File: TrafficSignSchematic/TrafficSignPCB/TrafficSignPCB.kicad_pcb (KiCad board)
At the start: 2 copper layers, 106.7 x 90.4 mm, 33 parts, among them J1 IDC connector, J2 3.96mm pitch 4-pin polarized 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, J3 Power In, U1 ATmega328P-PU, U2 SIM800L, Y1 16MHz

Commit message: Forgot to save...
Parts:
- moved R5 10.4 mm to (95.2, 151.6), turned to 180 degrees
- moved R4 2.55 mm to (108.7, 138.9)
- moved R6 2.55 mm to (101.1, 142.7)
- moved R3 2.55 mm to (101.1, 135.4)
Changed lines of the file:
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@@
   )
   (module Resistor_THT:R_Axial_DIN0204_L3.6mm_D1.6mm_P7.62mm_Horizontal (layer F.Cu)
-    (at 98.552 135.636)
+    (at 101.092 135.382)
     (descr "Resistor, Axial_DIN0204 series, Axial, Horizontal, pin pitch=7.62mm, 0.167W, length*diameter=3.6*1.6mm^2, http://cdn-reichelt.de/documents/datenblatt/B400/1_4W%23YAG.pdf")
     (tags "Resistor Axial_DIN0204 series Axial Horizontal pin pitch 7.62mm 0.167W length 3.6mm diameter 1.6mm")
@@
   )
   (module Resistor_THT:R_Axial_DIN0204_L3.6mm_D1.6mm_P7.62mm_Horizontal (layer F.Cu)
-    (at 106.172 139.192 180)
+    (at 108.712 138.938 180)
     (descr "Resistor, Axial_DIN0204 series, Axial, Horizontal, pin pitch=7.62mm, 0.167W, length*diameter=3.6*1.6mm^2, http://cdn-reichelt.de/documents/datenblatt/B400/1_4W%23YAG.pdf")
     (tags "Resistor Axial_DIN0204 series Axial Horizontal pin pitch 7.62mm 0.167W length 3.6mm diameter 1.6mm")
@@
   )
   (module Resistor_THT:R_Axial_DIN0204_L3.6mm_D1.6mm_P7.62mm_Horizontal (layer F.Cu)
-    (at 88.138 144.018 270)
+    (at 95.25 151.638 180)
     (descr "Resistor, Axial_DIN0204 series, Axial, Horizontal, pin pitch=7.62mm, 0.167W, length*diameter=3.6*1.6mm^2, http://cdn-reichelt.de/documents/datenblatt/B400/1_4W%23YAG.pdf")
     (tags "Resistor Axial_DIN0204 series Axial Horizontal pin pitch 7.62mm 0.167W length 3.6mm diameter 1.6mm")
-    (fp_text reference R5 (at 3.81 -1.92 90) (layer F.SilkS)
+    (fp_text reference R5 (at 3.81 -1.92) (layer F.SilkS)
       (effects (font (size 1 1) (thickness 0.15)))
     )
-    (fp_text value 10k (at 3.81 1.92 90) (layer F.Fab)
+    (fp_text value 10k (at 3.81 1.92) (layer F.Fab)
       (effects (font (size 1 1) (thickness 0.15)))
     )
@@
     (fp_line (start 8.57 1.05) (end 8.57 -1.05) (layer F.CrtYd) (width 0.05))
     (fp_line (start 8.57 -1.05) (end -0.95 -1.05) (layer F.CrtYd) (width 0.05))
-    (fp_text user %R (at 3.81 0 90) (layer F.Fab)
+    (fp_text user %R (at 3.81 0) (layer F.Fab)
       (effects (font (size 0.72 0.72) (thickness 0.108)))
     )
-    (pad 1 thru_hole circle (at 0 0 270) (size 1.4 1.4) (drill 0.7) (layers *.Cu *.Mask)
+    (pad 1 thru_hole circle (at 0 0 180) (size 1.4 1.4) (drill 0.7) (layers *.Cu *.Mask)
       (net 8 +5V))
-    (pad 2 thru_hole oval (at 7.62 0 270) (size 1.4 1.4) (drill 0.7) (layers *.Cu *.Mask)
+    (pad 2 thru_hole oval (at 7.62 0 180) (size 1.4 1.4) (drill 0.7) (layers *.Cu *.Mask)
       (net 40 "Net-(R5-Pad2)"))
     (model ${KISYS3DMOD}/Resistor_THT.3dshapes/R_Axial_DIN0204_L3.6mm_D1.6mm_P7.62mm_Horizontal.wrl
@@
   )
   (module Resistor_THT:R_Axial_DIN0204_L3.6mm_D1.6mm_P7.62mm_Horizontal (layer F.Cu)
-    (at 98.552 143.002)
+    (at 101.092 142.748)
     (descr "Resistor, Axial_DIN0204 series, Axial, Horizontal, pin pitch=7.62mm, 0.167W, length*diameter=3.6*1.6mm^2, http://cdn-reichelt.de/documents/datenblatt/B400/1_4W%23YAG.pdf")
     (tags "Resistor Axial_DIN0204 series Axial Horizontal pin pitch 7.62mm 0.167W length 3.6mm diameter 1.6mm")

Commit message: Moving elements
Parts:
- added H1: MountingHole, MountingHole:MountingHole_3.2mm_M3_ISO14580, F.Cu at (51.4, 70.5)
- added H2: MountingHole, MountingHole:MountingHole_3.2mm_M3_ISO14580, F.Cu at (52.1, 151.8)
- added H3: MountingHole, MountingHole:MountingHole_3.2mm_M3_ISO14580, F.Cu at (149.9, 152.4)
- added H4: MountingHole, MountingHole:MountingHole_3.2mm_M3_ISO14580, F.Cu at (149.9, 69.8)
- moved G*** 64.6 mm to (108.6, 118.1)
- moved CFF1 15.5 mm to (142.2, 99.1), turned to 0 degrees
- moved R1 9.44 mm to (147.3, 102.9), turned to 270 degrees
- moved VR1 5.46 mm to (135.3, 88.3)
- moved J1 4.71 mm to (57.1, 140.3)
- moved CIN2 4.27 mm to (118.7, 82.5)
- moved C2 4.07 mm to (89.7, 128.1)
- moved C3 4.07 mm to (73.8, 130.4)
- moved C4 4.07 mm to (73.8, 127.4)
- moved R5 4.07 mm to (97.8, 148.5)
- moved U1 4.07 mm to (85.1, 148.5)
- moved C1 4.07 mm to (89.7, 120.3)
- moved R7 4.07 mm to (85.1, 109.9)
- moved Y1 4.07 mm to (95.5, 119.3)
- moved C5 4.07 mm to (88.1, 133.2)
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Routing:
- net OE: track 22.3 -> 0.00 mm
- net +12V: track 3.96 -> 0.00 mm

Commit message: PCB v3
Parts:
- Power In: renamed from J3
- moved G*** 31.8 mm to (106.2, 149.9)
- moved R3 17.2 mm to (86.1, 139.7)
- moved R6 16.4 mm to (86.1, 143.4)
- moved R4 12.2 mm to (97.9, 139.7), turned to 0 degrees
- moved C7 7.04 mm to (69.3, 102.5), turned to 180 degrees
- moved C2 6.48 mm to (86.9, 122.3), turned to 270 degrees
- moved C1 6.36 mm to (86.9, 114.6), turned to 270 degrees
- moved CFF1 6.02 mm to (148.2, 99.8), turned to 180 degrees
- moved COUT1 4.84 mm to (123.2, 121.9), turned to 90 degrees
- moved R5 4.13 mm to (93.7, 147.7)
- moved C5 3.61 mm to (85.3, 130.9)
- moved Y1 2.90 mm to (92.7, 118.5)
- moved C4 2.90 mm to (71.0, 126.6)
- moved R7 2.90 mm to (82.3, 109.1)
- moved U1 2.90 mm to (82.3, 147.7)
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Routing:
- net +5V: track 0.00 -> 184.2 mm
- net G1: track 0.00 -> 105.7 mm
- net +12V: track 0.00 -> 83.4 mm
- net B0: track 0.00 -> 76.9 mm
- net B1: track 0.00 -> 71.8 mm
- net +4V: track 0.00 -> 69.8 mm
- net R1: track 0.00 -> 66.9 mm
- net GND: track 0.00 -> 64.0 mm, vias 0 -> 104
- net G0: track 0.00 -> 63.4 mm
- net SIM_RST: track 0.00 -> 57.8 mm
- net R0: track 0.00 -> 46.1 mm
- net Net-(R3-Pad2): track 0.00 -> 45.6 mm
- net Net-(R6-Pad2): track 0.00 -> 43.0 mm
- net D: track 0.00 -> 38.5 mm
- net C: track 0.00 -> 36.5 mm
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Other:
- rule trace_min: 0.2032 -> 0.2286

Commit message: Added images
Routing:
- net GND: track 64.0 -> 76.1 mm
- net +5V: track 184.2 -> 184.9 mm
- added copper zone on F.Cu, net GND
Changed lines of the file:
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@@
     (thickness 1.6)
     (drawings 8)
-    (tracks 378)
+    (tracks 381)
     (zones 0)
     (modules 37)
@@
   (page A4)
   (layers
-    (0 F.Cu signal)
+    (0 F.Cu signal hide)
     (31 B.Cu signal hide)
     (32 B.Adhes user)
@@
   )
   (setup
-    (last_trace_width 3.175)
+    (last_trace_width 1.27)
     (user_trace_width 0.3048)
     (user_trace_width 0.381)
@@
   (via (at 123.19 102.87) (size 1.2) (drill 0.8) (layers F.Cu B.Cu) (net 2))
   (via (at 123.19 105.41) (size 1.2) (drill 0.8) (layers F.Cu B.Cu) (net 2))
-  (via (at 58.42 76.2) (size 1.2) (drill 0.8) (layers F.Cu B.Cu) (net 2))
-  (via (at 60.96 81.28) (size 1.2) (drill 0.8) (layers F.Cu B.Cu) (net 2))
-  (via (at 68.58 78.74) (size 1.2) (drill 0.8) (layers F.Cu B.Cu) (net 2))
-  (via (at 58.42 78.74) (size 1.2) (drill 0.8) (layers F.Cu B.Cu) (net 2))
-  (via (at 63.5 81.28) (size 1.2) (drill 0.8) (layers F.Cu B.Cu) (net 2))
-  (via (at 68.58 76.2) (size 1.2) (drill 0.8) (layers F.Cu B.Cu) (net 2))
-  (via (at 68.58 81.28) (size 1.2) (drill 0.8) (layers F.Cu B.Cu) (net 2))
-  (via (at 68.58 83.82) (size 1.2) (drill 0.8) (layers F.Cu B.Cu) (net 2))
-  (via (at 60.96 76.2) (size 1.2) (drill 0.8) (layers F.Cu B.Cu) (net 2))
-  (via (at 63.5 78.74) (size 1.2) (drill 0.8) (layers F.Cu B.Cu) (net 2))
-  (via (at 66.04 83.82) (size 1.2) (drill 0.8) (layers F.Cu B.Cu) (net 2))
-  (via (at 63.5 83.82) (size 1.2) (drill 0.8) (layers F.Cu B.Cu) (net 2))
-  (via (at 66.04 76.2) (size 1.2) (drill 0.8) (layers F.Cu B.Cu) (net 2))
-  (via (at 63.5 83.82) (size 1.2) (drill 0.8) (layers F.Cu B.Cu) (net 2))
-  (via (at 63.5 76.2) (size 1.2) (drill 0.8) (layers F.Cu B.Cu) (net 2))
-  (via (at 60.96 78.74) (size 1.2) (drill 0.8) (layers F.Cu B.Cu) (net 2))
-  (via (at 66.04 78.74) (size 1.2) (drill 0.8) (layers F.Cu B.Cu) (net 2))
-  (via (at 66.04 81.28) (size 1.2) (drill 0.8) (layers F.Cu B.Cu) (net 2))
-  (via (at 60.96 83.82) (size 1.2) (drill 0.8) (layers F.Cu B.Cu) (net 2))
-  (via (at 58.42 83.82) (size 1.2) (drill 0.8) (layers F.Cu B.Cu) (net 2))
-  (via (at 58.42 81.28) (size 1.2) (drill 0.8) (layers F.Cu B.Cu) (net 2))
+  (via (at 59.69 85.09) (size 1.2) (drill 0.8) (layers F.Cu B.Cu) (net 2))
+  (via (at 64.77 82.55) (size 1.2) (drill 0.8) (layers F.Cu B.Cu) (net 2))
+  (via (at 62.23 74.93) (size 1.2) (drill 0.8) (layers F.Cu B.Cu) (net 2))
+  (via (at 62.23 85.09) (size 1.2) (drill 0.8) (layers F.Cu B.Cu) (net 2))
+  (via (at 64.77 80.01) (size 1.2) (drill 0.8) (layers F.Cu B.Cu) (net 2))
+  (via (at 59.69 74.93) (size 1.2) (drill 0.8) (layers F.Cu B.Cu) (net 2))
+  (via (at 64.77 74.93) (size 1.2) (drill 0.8) (layers F.Cu B.Cu) (net 2))
+  (via (at 67.31 74.93) (size 1.2) (drill 0.8) (layers F.Cu B.Cu) (net 2))
+  (via (at 59.69 82.55) (size 1.2) (drill 0.8) (layers F.Cu B.Cu) (net 2))
+  (via (at 62.23 80.01) (size 1.2) (drill 0.8) (layers F.Cu B.Cu) (net 2))
+  (via (at 67.31 77.47) (size 1.2) (drill 0.8) (layers F.Cu B.Cu) (net 2))
+  (via (at 67.31 80.01) (size 1.2) (drill 0.8) (layers F.Cu B.Cu) (net 2))
+  (via (at 59.69 77.47) (size 1.2) (drill 0.8) (layers F.Cu B.Cu) (net 2))
+  (via (at 67.31 80.01) (size 1.2) (drill 0.8) (layers F.Cu B.Cu) (net 2))
+  (via (at 59.69 80.01) (size 1.2) (drill 0.8) (layers F.Cu B.Cu) (net 2))
+  (via (at 62.23 82.55) (size 1.2) (drill 0.8) (layers F.Cu B.Cu) (net 2))
+  (via (at 62.23 77.47) (size 1.2) (drill 0.8) (layers F.Cu B.Cu) (net 2))
+  (via (at 64.77 77.47) (size 1.2) (drill 0.8) (layers F.Cu B.Cu) (net 2))
+  (via (at 67.31 82.55) (size 1.2) (drill 0.8) (layers F.Cu B.Cu) (net 2))
+  (via (at 67.31 85.09) (size 1.2) (drill 0.8) (layers F.Cu B.Cu) (net 2))
+  (via (at 64.77 85.09) (size 1.2) (drill 0.8) (layers F.Cu B.Cu) (net 2))
   (via (at 144.145 86.995) (size 1.2) (drill 0.8) (layers F.Cu B.Cu) (net 2))
   (via (at 141.605 86.995) (size 1.2) (drill 0.8) (layers F.Cu B.Cu) (net 2))
@@
   (segment (start 141.068 88.671) (end 137.668 85.271) (width 1.27) (layer F.Cu) (net 2))
   (segment (start 141.068 94.421) (end 141.068 88.671) (width 1.27) (layer F.Cu) (net 2))
-  (segment (start 137.668 107.442) (end 132.715 112.395) (width 1.27) (layer F.Cu) (net 2))
-  (segment (start 137.668 94.421) (end 137.668 107.442) (width 1.27) (layer F.Cu) (net 2))
   (segment (start 85.411 95.504) (end 94.561 95.504) (width 1.27) (layer F.Cu) (net 2))
+  (segment (start 135.255 112.395) (end 132.715 112.395) (width 1.27) (layer F.Cu) (net 2))
+  (segment (start 137.668 94.421) (end 137.668 109.982) (width 1.27) (layer F.Cu) (net 2))
+  (segment (start 137.668 109.982) (end 135.255 112.395) (width 1.27) (layer F.Cu) (net 2))
+  (segment (start 91.161 98.904) (end 94.561 95.504) (width 1.27) (layer F.Cu) (net 2))
+  (segment (start 85.411 98.904) (end 91.161 98.904) (width 1.27) (layer F.Cu) (net 2))
   (segment (start 85.297 119.554) (end 86.868 119.554) (width 0.381) (layer F.Cu) (net 3))
   (segment (start 84.709 120.142) (end 85.297 119.554) (width 0.381) (layer F.Cu) (net 3))
@@
   (segment (start 73.279 106.172) (end 74.549 107.442) (width 0.635) (layer F.Cu) (net 8))
   (segment (start 73.279 103.632) (end 73.279 106.172) (width 0.635) (layer F.Cu) (net 8))
-  (segment (start 55.245 86.995) (end 55.245 80.415) (width 3.175) (layer F.Cu) (net 8))
+  (segment (start 55.245 88.265) (end 55.245 80.415) (width 3.175) (layer F.Cu) (net 8))
+  (segment (start 57.15 90.17) (end 55.245 88.265) (width 3.175) (layer F.Cu) (net 8))
+  (segment (start 69.262 102.489) (end 69.215 102.442) (width 3.175) (layer F.Cu) (net 8))
   (segment (start 69.215 102.442) (end 69.215 92.545) (width 3.175) (layer F.Cu) (net 8))
-  (segment (start 69.262 102.489) (end 69.215 102.442) (width 3.175) (layer F.Cu) (net 8))
   (segment (start 69.215 92.545) (end 66.84 90.17) (width 3.175) (layer F.Cu) (net 8))
-  (segment (start 66.84 90.17) (end 58.42 90.17) (width 3.175) (layer F.Cu) (net 8))
-  (segment (start 58.42 90.17) (end 55.245 86.995) (width 3.175) (layer F.Cu) (net 8))
+  (segment (start 66.84 90.17) (end 57.15 90.17) (width 3.175) (layer F.Cu) (net 8))
   (segment (start 135.185 99.695) (end 132.715 99.695) (width 1.27) (layer F.Cu) (net 9))
   (segment (start 135.968 98.912) (end 135.185 99.695) (width 1.27) (layer F.Cu) (net 9))
   (segment (start 135.968 94.421) (end 135.968 98.912) (width 1.27) (layer F.Cu) (net 9))
-  (segment (start 132.715 99.695) (end 129.54 99.695) (width 1.905) (layer F.Cu) (net 9))
-  (segment (start 123.595 93.75) (end 118.11 93.75) (width 1.905) (layer F.Cu) (net 9))
-  (segment (start 129.54 99.695) (end 123.595 93.75) (width 1.905) (layer F.Cu) (net 9))
+  (segment (start 126.135 93.75) (end 118.11 93.75) (width 1.905) (layer F.Cu) (net 9))
+  (segment (start 132.715 99.695) (end 132.08 99.695) (width 1.905) (layer F.Cu) (net 9))
+  (segment (start 132.08 99.695) (end 126.135 93.75) (width 1.905) (layer F.Cu) (net 9))
   (segment (start 76.708 92.456) (end 76.708 89.408) (width 1.27) (layer F.Cu) (net 10))
   (segment (start 85.411 93.804) (end 78.056 93.804) (width 1.27) (layer F.Cu) (net 10))
@@
       )
     )
+  )
+  (zone (net 2) (net_name GND) (layer F.Cu) (hatch edge 0.508)
+    (connect_pads (clearance 0.508))
+    (min_thickness 0.254)
+    (fill yes (arc_segments 32) (thermal_gap 0.508) (thermal_bridge_width 0.508))
+    (polygon
+      (pts
+        (xy 68.58 87.63) (xy 58.42 87.63) (xy 58.42 72.39) (xy 68.58 72.39)
+      )
+    )
+  )
+  (zone (net 2) (net_name GND) (layer F.Cu) (hatch edge 0.508)
+    (connect_pads (clearance 0.508))
+    (min_thickness 0.254)
+    (fill yes (arc_segments 32) (thermal_gap 0.508) (thermal_bridge_width 0.508))
+    (polygon
+      (pts
+        (xy 125.73 106.68) (xy 110.49 106.68) (xy 110.49 96.52) (xy 125.73 96.52)
+      )
+    )

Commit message: Working admin app multithreading
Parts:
- Matrix Control: renamed from J1
- Matrix Power: renamed from J2
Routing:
- net /RXD: track 5.07 -> 4.55 mm

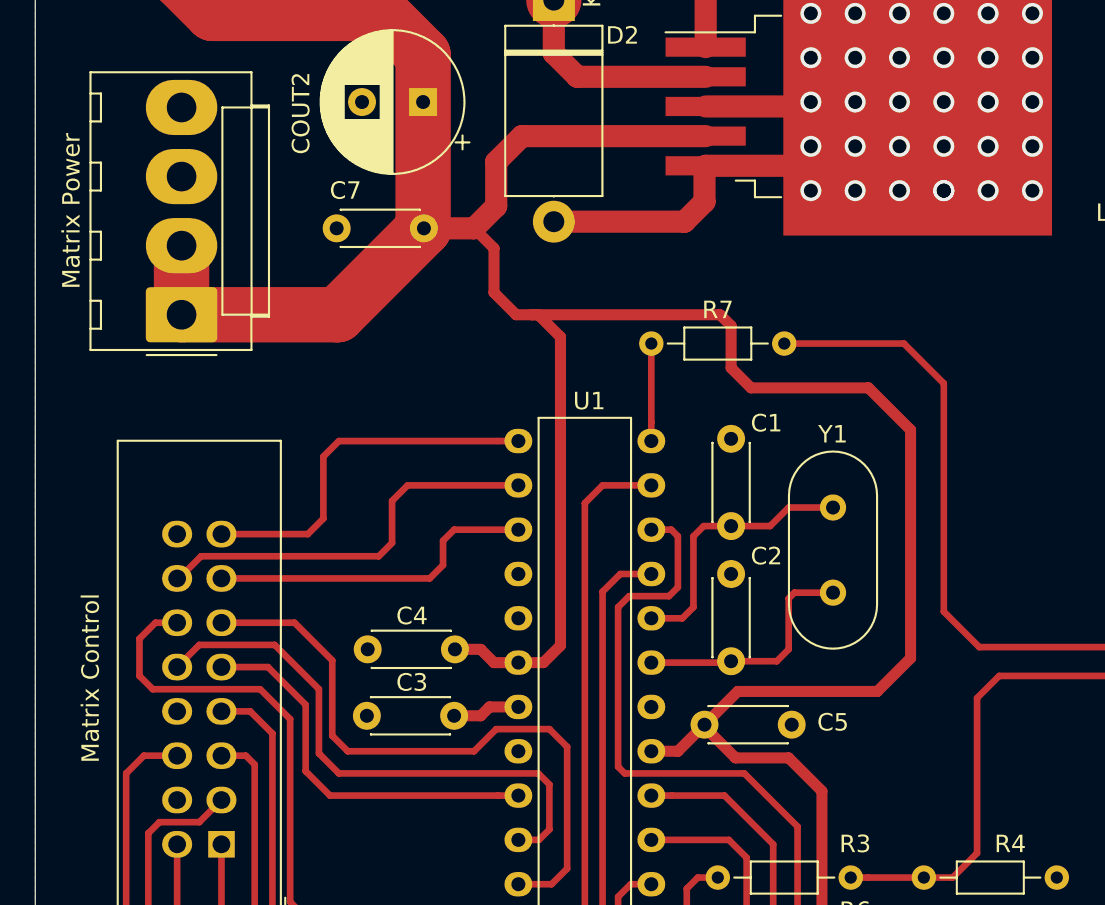
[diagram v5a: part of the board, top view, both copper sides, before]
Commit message: Updated the PCB schematic and layout
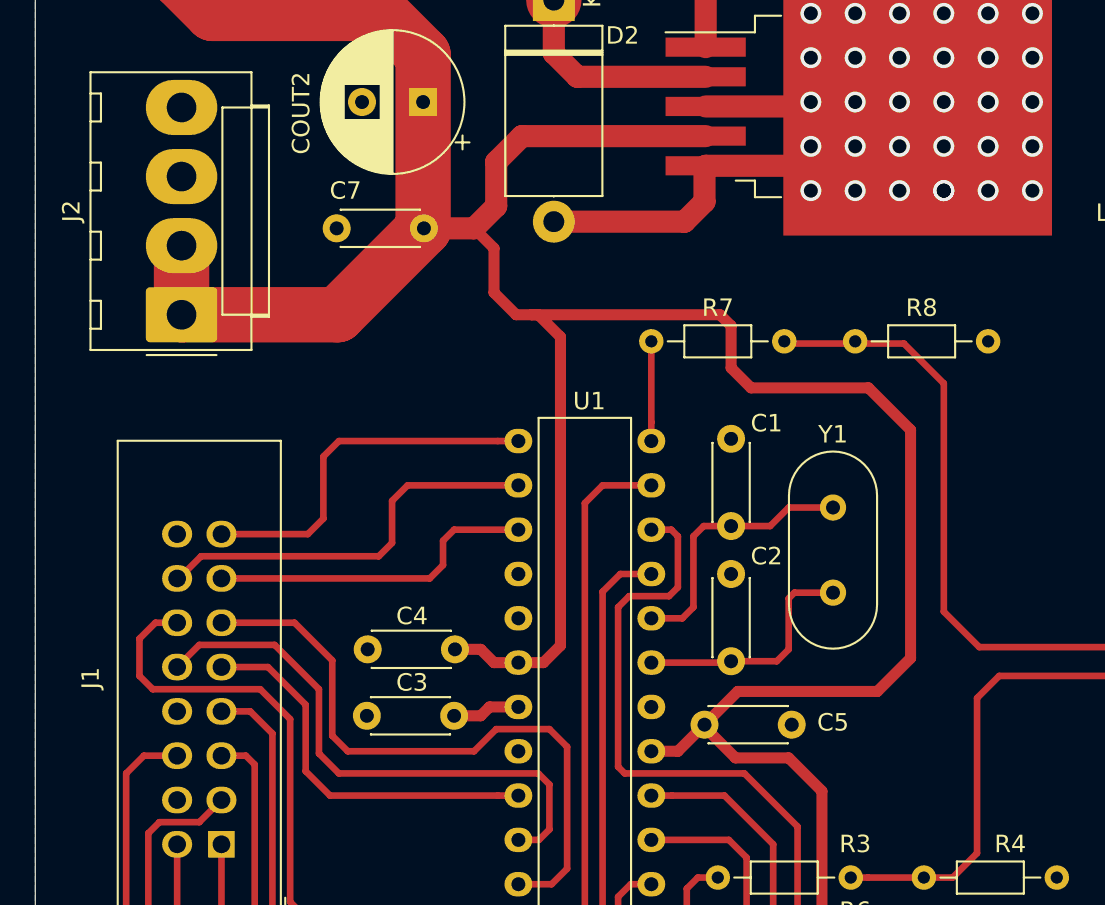
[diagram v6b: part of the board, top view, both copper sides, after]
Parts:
- added R8: 20k, Resistor_THT:R_Axial_DIN0204_L3.6mm_D1.6mm_P7.62mm_Horizontal, F.Cu at (94.0, 109.0)
- C6, C7: value 100n -> 100nF
- CIN1, CIN2: value 680uF -> 35V/680uF
- COUT1: value 470uF -> 16V/470uF
- COUT2: value 330uF -> 25V/330uF
- J1: renamed from Matrix Control; value IDC connector -> LED matrix data
- J2: renamed from Matrix Power; value 3.96mm pitch 4-pin polarized connector -> LED matrix power
- R2: value 2.2k/1% -> 2.21k/1%
- R3, R7: value 10k -> 16k
- moved R7 0.13 mm to (82.3, 109.0)
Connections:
- net /RXD renamed SIM_TX
- net /TXD renamed SIM_RX
- R7 pad 1: /8 -> SIM_RST
- R7 pad 2: SIM_RST -> Net-(R7-Pad2)
- U1 pad 14: /8 -> SIM_RST
- U2 pad 3: SIM_RST -> Net-(R7-Pad2)
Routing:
- net Net-(R7-Pad2): track 0.00 -> 57.8 mm
- net SIM_RST: track 57.8 -> 5.59 mm
- net /8: track 5.59 -> 0.00 mm

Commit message: Made small adjustments to PCB design
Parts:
- removed Power In: Power In, Connector_Molex:Molex_KK-396_A-41791-0004_1x04_P3.96mm_Vertical
- added J3: Power In, Connector_Molex:Molex_KK-396_A-41791-0004_1x04_P3.96mm_Vertical, F.Cu at (95.8, 74.9)
